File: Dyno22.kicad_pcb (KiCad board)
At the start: 2 copper layers, 160 x 110 mm, 43 parts, among them J1 Pwr Input, J2 Display, J3 Pwr Output, J4 BPM & Sensors, J6 Encoder, J7 UART, U1 TS2937CW50, U2 LM324, U3 74HC4052

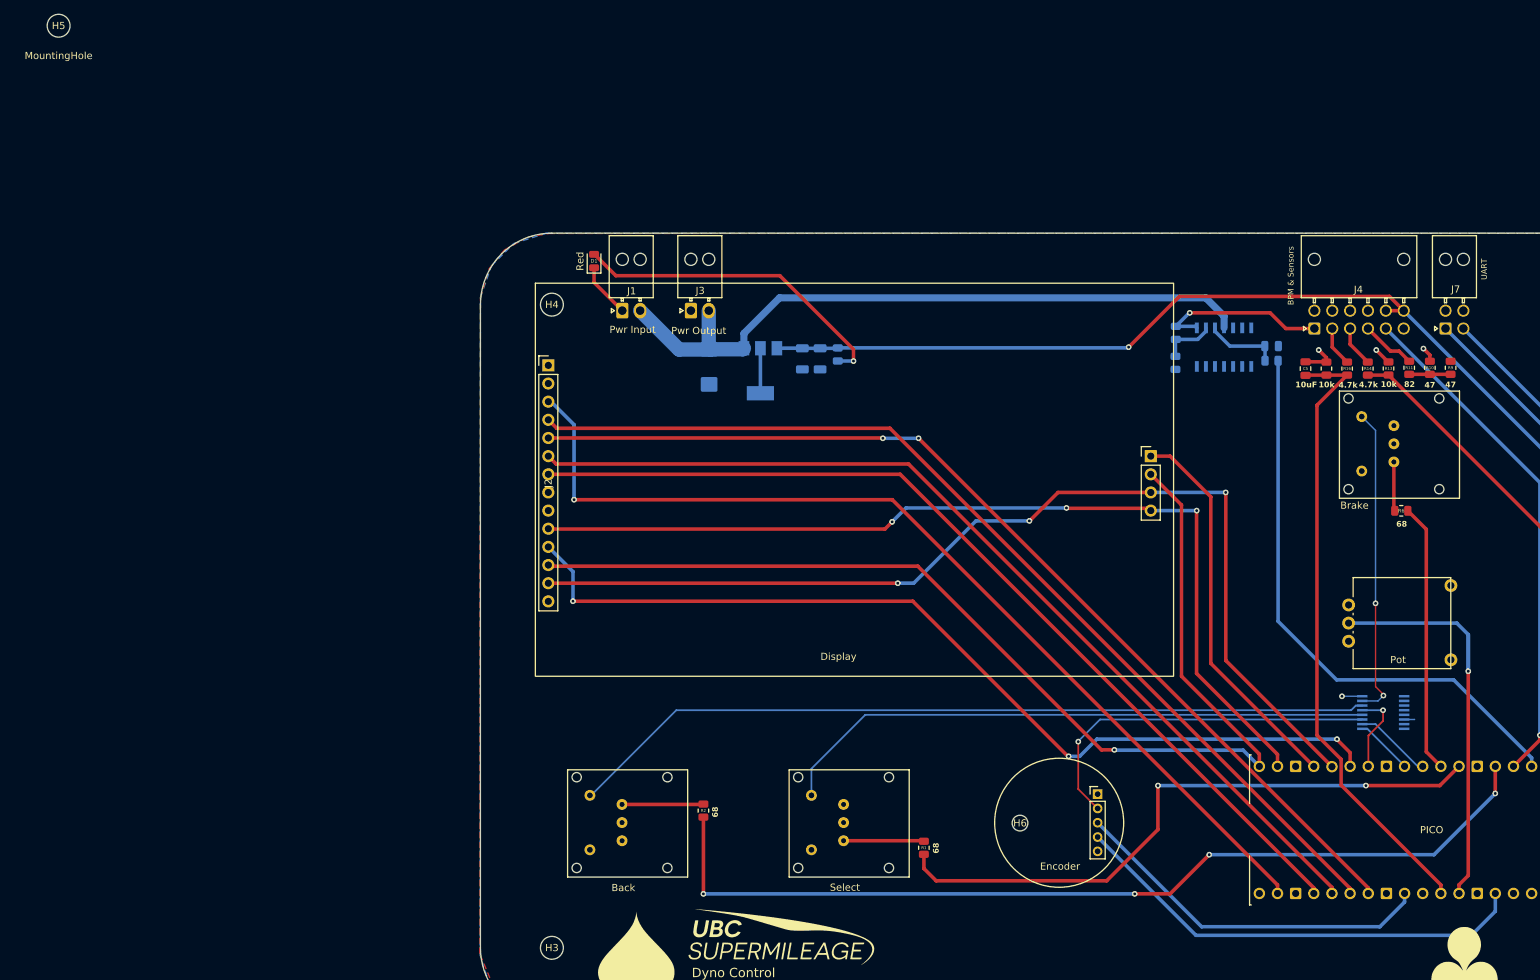
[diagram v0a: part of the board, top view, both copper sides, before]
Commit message: Fix Rotary Encoder Footprint #14
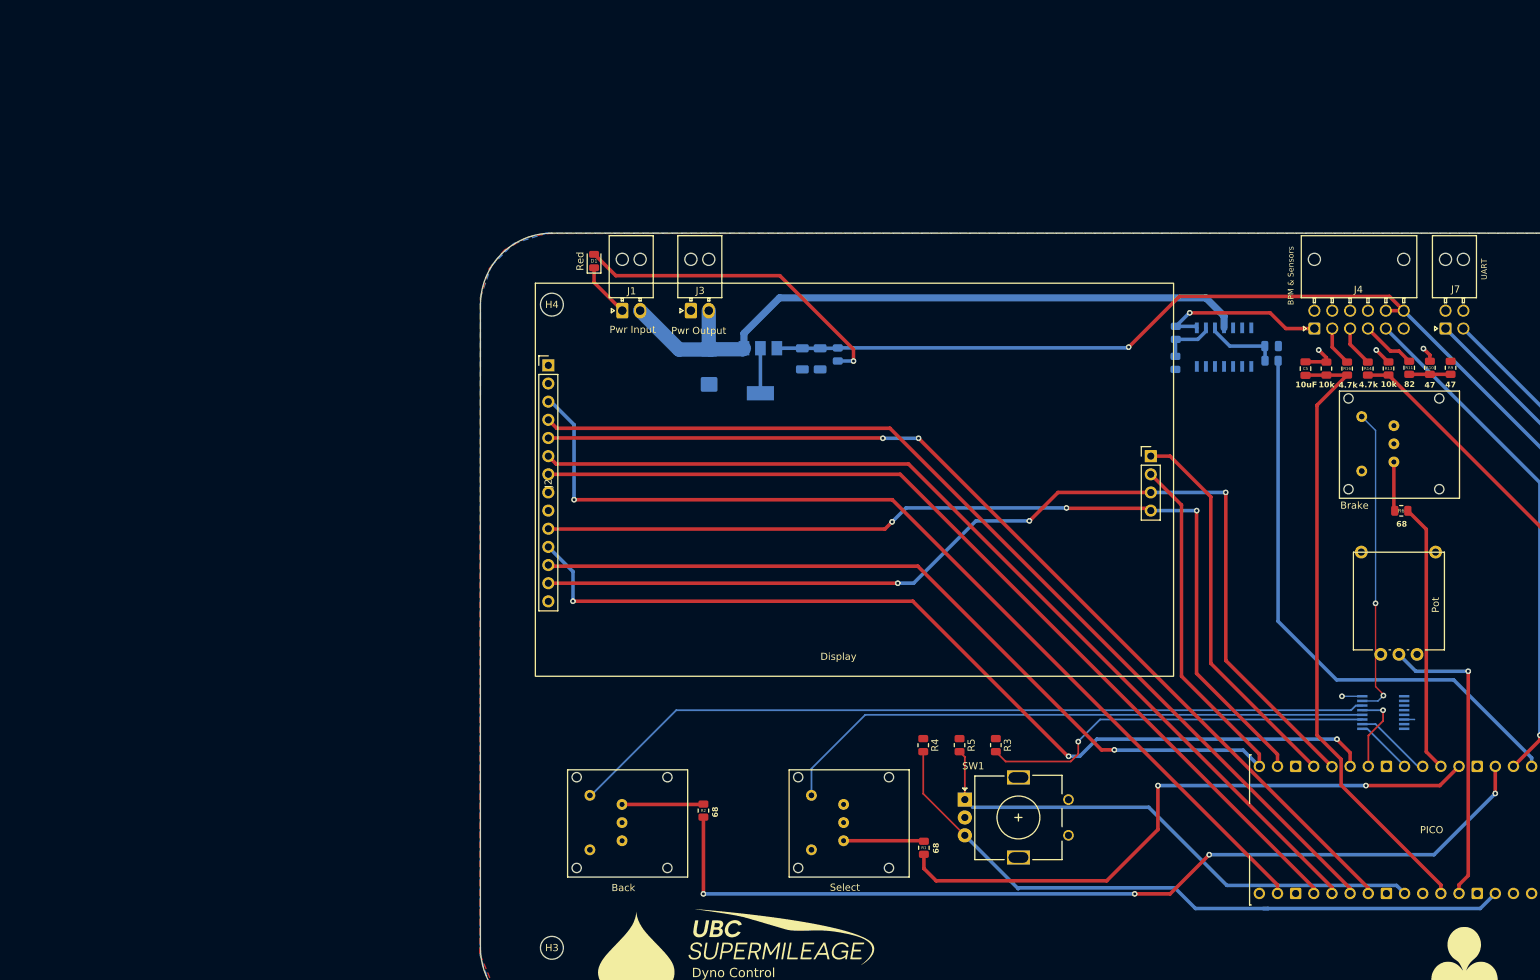
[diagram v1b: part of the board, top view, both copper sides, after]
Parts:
- removed H5: MountingHole, MountingHole:MountingHole_3.2mm_M3
- removed H6: MountingHole, MountingHole:MountingHole_2.2mm_M2
- removed J6: Encoder, custom_connectors:RotaryEncoder_Dyno
- added R3: 5kΩ, Resistor_SMD:R_0805_2012Metric, F.Cu at (134.6, 104.1)
- added R4: 5kΩ, Resistor_SMD:R_0805_2012Metric, F.Cu at (124.5, 104.1)
- added R5: 5kΩ, Resistor_SMD:R_0805_2012Metric, F.Cu at (129.5, 104.1)
- added SW1: RotaryEncoder_Switch, Rotary_Encoder:RotaryEncoder_Alps_EC11E_Vertical_H20mm, F.Cu at (130.3, 111.8)
- C4: value 22uF -> 22 uF
- moved RV1 10.0 mm to (184.7, 90.7), turned to 90 degrees
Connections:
- A1 pad 29: /ROT_EN_A -> /ROT_EN_B
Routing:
- net /ROT_EN_B: track 65.2 -> 168.3 mm
- net /ROT_EN_A: track 51.6 -> 0.00 mm
- net /BPM_CTRL_IN: track 59.3 -> 42.3 mm
- net /ROT_EN_SW: track 51.6 -> 55.4 mm

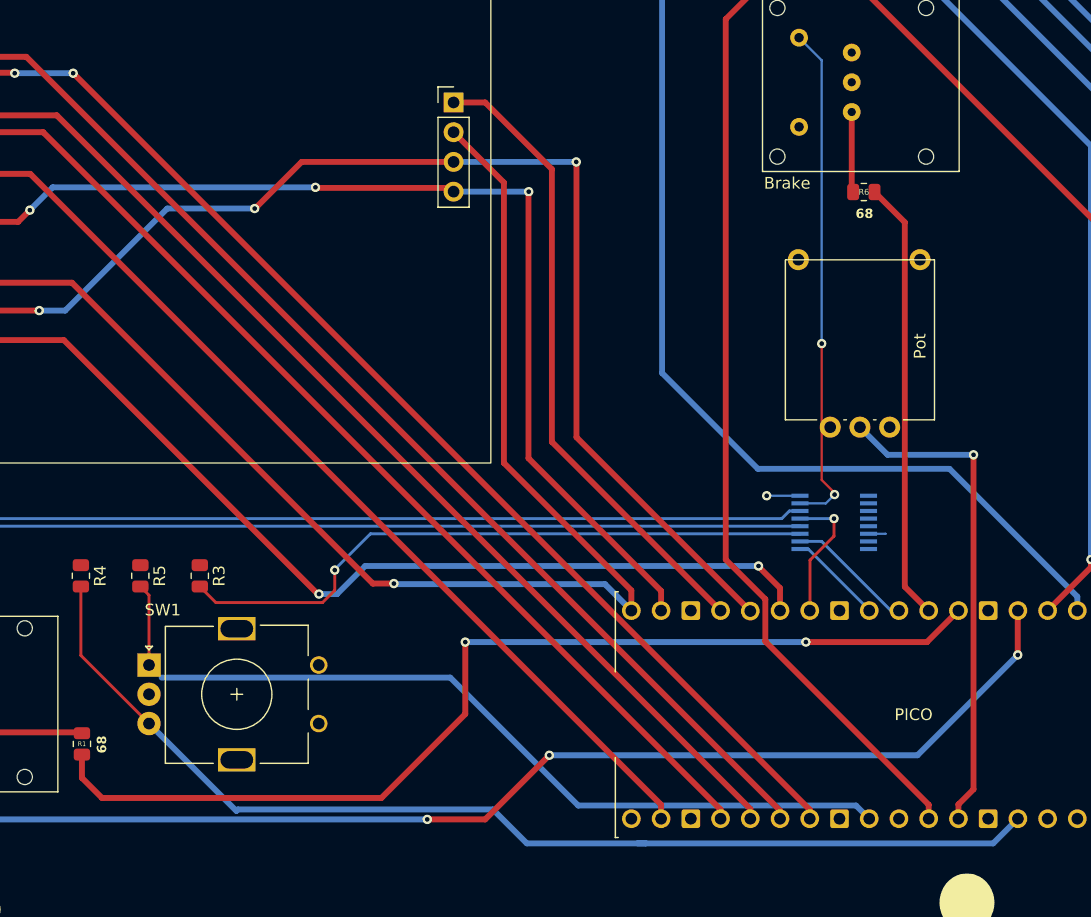
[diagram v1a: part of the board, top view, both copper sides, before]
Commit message: Rerouted some traces for DRC and made ROT pins consecutive
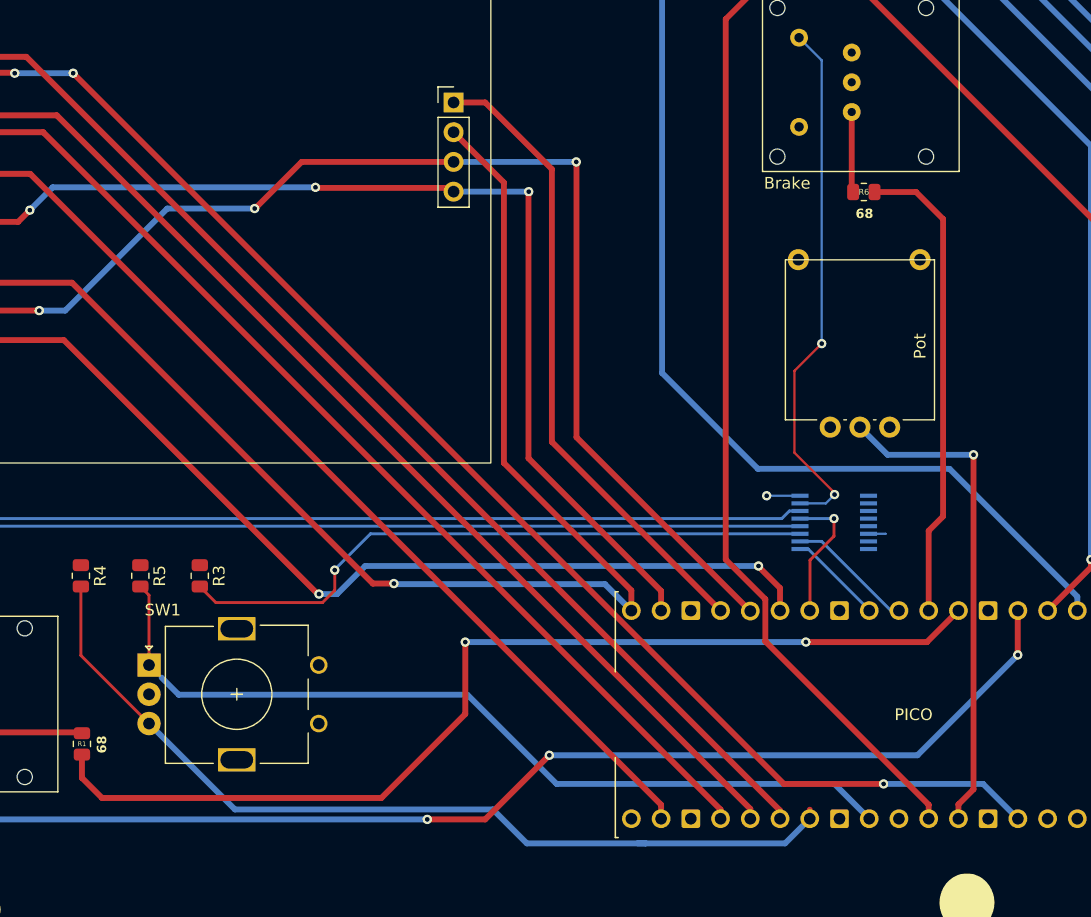
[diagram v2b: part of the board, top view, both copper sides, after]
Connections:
- A1 pad 27: /LCD_DC -> /ROT_EN_B
- A1 pad 29: /ROT_EN_B -> /ROT_EN_A
- A1 pad 34: /ROT_EN_B -> /LCD_DC
- R5 pad 2: /ROT_EN_B -> /ROT_EN_A
- SW1 pad A: /ROT_EN_B -> /ROT_EN_A
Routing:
- net /ROT_EN_B: track 168.3 -> 77.2 mm
- net /ROT_EN_A: track 0.00 -> 74.0 mm
- net /LCD_DC: track 141.6 -> 158.9 mm, vias 2 -> 3
- net /LED_BRAKE: track 37.7 -> 40.8 mm
- net /BTN_BRAKE: track 43.8 -> 45.7 mm

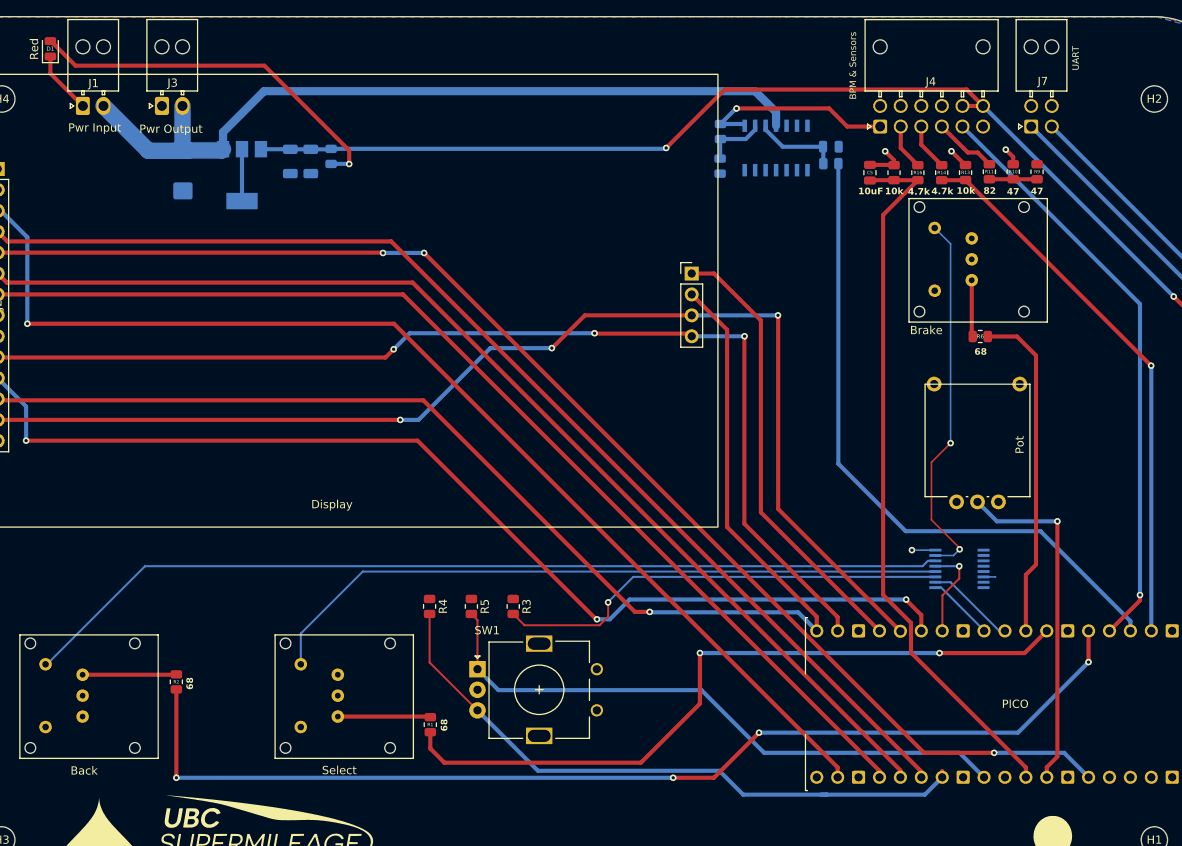
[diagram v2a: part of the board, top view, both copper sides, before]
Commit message: Changes the rotary encoder input pins, spacing adjustments to encoder and potentiometer, increase in silkscreen text size.
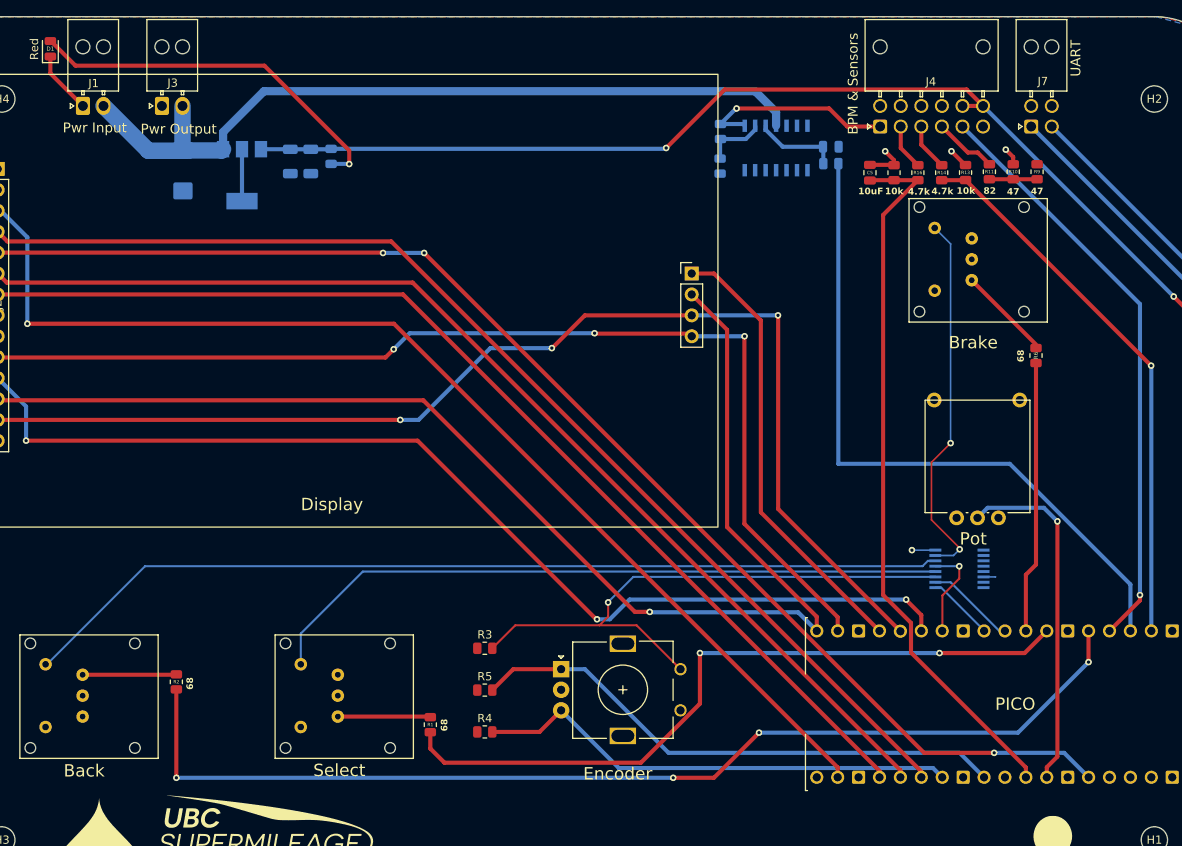
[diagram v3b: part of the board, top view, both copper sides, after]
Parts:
- moved R4 16.7 mm to (131.2, 119.4), turned to 0 degrees
- moved R5 10.3 mm to (131.2, 114.3), turned to 0 degrees
- moved Encoder 10.2 mm to (140.4, 111.8)
- moved R6 7.15 mm to (198.1, 73.7), turned to -90 degrees
- moved R3 6.14 mm to (131.2, 109.2), turned to 0 degrees
- moved RV1 1.94 mm to (184.7, 92.7)
- renumbered SW1 to Encoder
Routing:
- net /ROT_EN_B: track 77.2 -> 59.1 mm
- net /ROT_EN_SW: track 55.4 -> 70.6 mm
- net /ROT_EN_A: track 74.0 -> 66.2 mm
- net /LED_BRAKE: track 40.8 -> 33.0 mm
- net Net-(S3-L1_Y): track 6.89 -> 11.5 mm
- net /BPM_CTRL_OUT: track 81.0 -> 83.7 mm
